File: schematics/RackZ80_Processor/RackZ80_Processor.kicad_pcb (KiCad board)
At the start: 2 copper layers, 160 x 100 mm, 2 parts

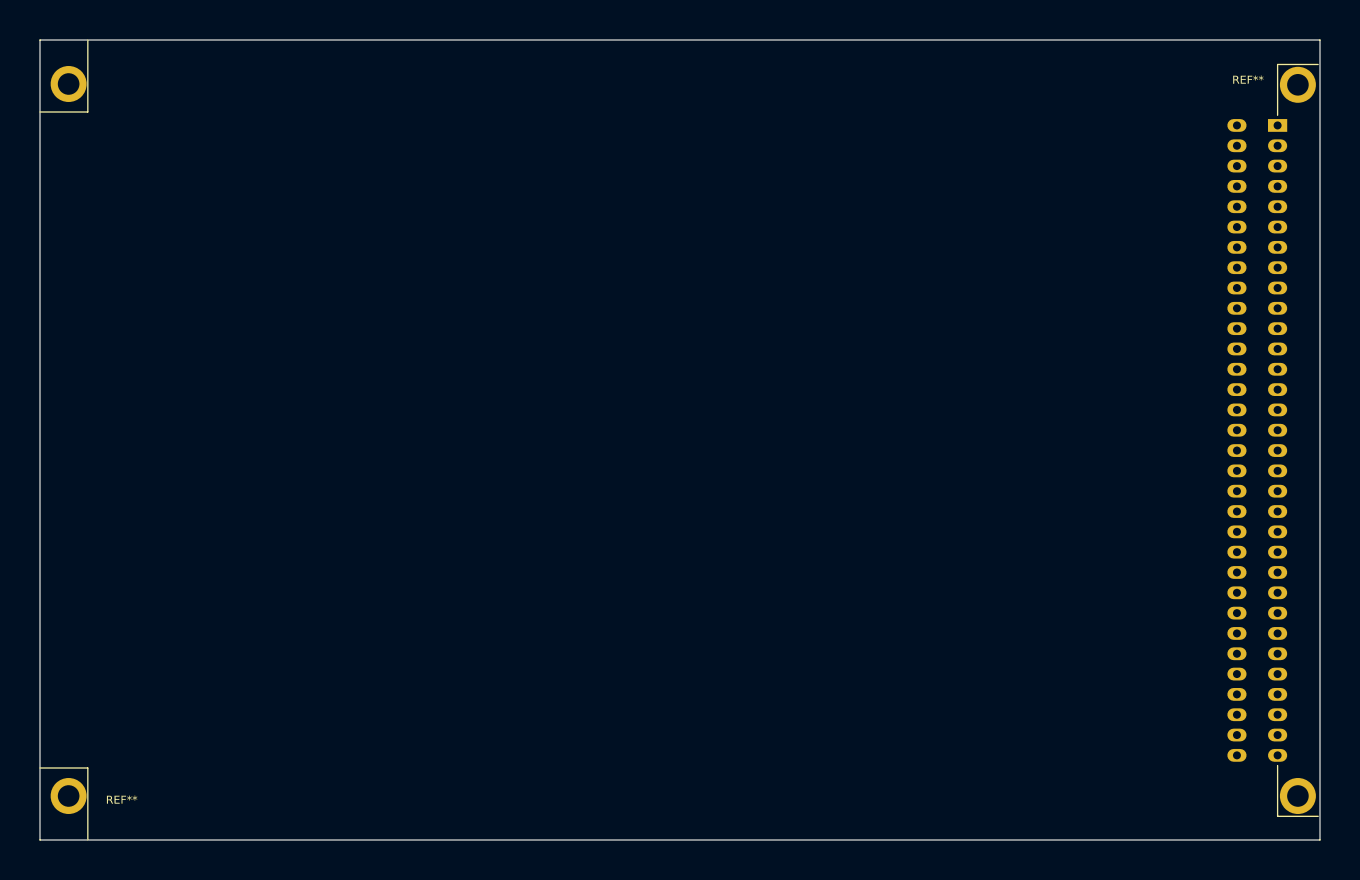
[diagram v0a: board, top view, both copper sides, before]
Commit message: schematics update
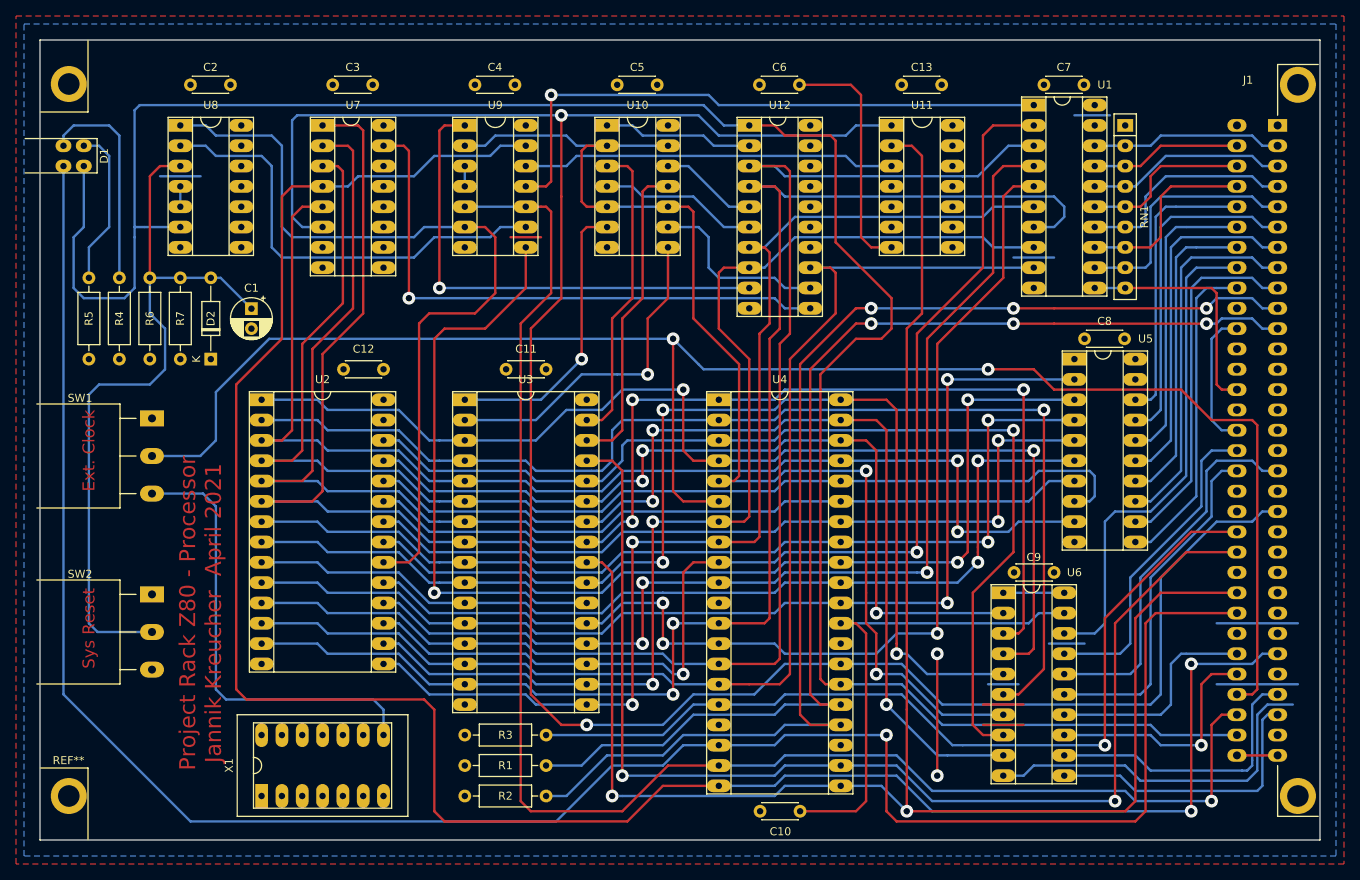
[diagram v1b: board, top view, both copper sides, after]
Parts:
- removed the REF** at (226.8, 138.2)
- added C1: 10uF, Capacitor_THT:CP_Radial_D5.0mm_P2.50mm, F.Cu at (93.2, 71.8)
- added C10: 100nF, Capacitor_THT:C_Disc_D4.3mm_W1.9mm_P5.00mm, F.Cu at (156.8, 134.6)
- added C11: 100nF, Capacitor_THT:C_Disc_D4.3mm_W1.9mm_P5.00mm, F.Cu at (130.1, 79.4)
- added C12: 100nF, Capacitor_THT:C_Disc_D4.3mm_W1.9mm_P5.00mm, F.Cu at (109.7, 79.4)
- added C13: 100nF, Capacitor_THT:C_Disc_D4.3mm_W1.9mm_P5.00mm, F.Cu at (174.5, 43.8)
- added C2: 100nF, Capacitor_THT:C_Disc_D4.3mm_W1.9mm_P5.00mm, F.Cu at (85.6, 43.8)
- added C3: 100nF, Capacitor_THT:C_Disc_D4.3mm_W1.9mm_P5.00mm, F.Cu at (103.4, 43.8)
- added C4: 100nF, Capacitor_THT:C_Disc_D4.3mm_W1.9mm_P5.00mm, F.Cu at (121.2, 43.8)
- added C5: 100nF, Capacitor_THT:C_Disc_D4.3mm_W1.9mm_P5.00mm, F.Cu at (138.9, 43.8)
- added C6: 100nF, Capacitor_THT:C_Disc_D4.3mm_W1.9mm_P5.00mm, F.Cu at (156.7, 43.8)
- added C7: 100nF, Capacitor_THT:C_Disc_D4.3mm_W1.9mm_P5.00mm, F.Cu at (192.3, 43.8)
- added C8: 100nF, Capacitor_THT:C_Disc_D4.3mm_W1.9mm_P5.00mm, F.Cu at (197.4, 75.6)
- added C9: 100nF, Capacitor_THT:C_Disc_D4.3mm_W1.9mm_P5.00mm, F.Cu at (193.6, 104.8)
- added D1: LED, rackz80_footprints:LED_Array_2, F.Cu at (69.7, 51.4)
- added D2: D, Diode_THT:D_DO-35_SOD27_P10.16mm_Horizontal, F.Cu at (88.2, 78.1)
- added J1: ECB_Kontron, rackz80_footprints:Eurocard_DIN41612_C64_Male, F.Cu at (226.8, 138.2)
- added R1: 1k, Resistor_THT:R_Axial_DIN0207_L6.3mm_D2.5mm_P10.16mm_Horizontal, F.Cu at (130.1, 128.9)
- added R2: 1k, Resistor_THT:R_Axial_DIN0207_L6.3mm_D2.5mm_P10.16mm_Horizontal, F.Cu at (130.1, 132.7)
- added R3: 1k, Resistor_THT:R_Axial_DIN0207_L6.3mm_D2.5mm_P10.16mm_Horizontal, F.Cu at (130.1, 125.1)
- added R4: 1k, Resistor_THT:R_Axial_DIN0207_L6.3mm_D2.5mm_P10.16mm_Horizontal, F.Cu at (76.7, 78.1)
- added R5: 1k, Resistor_THT:R_Axial_DIN0207_L6.3mm_D2.5mm_P10.16mm_Horizontal, F.Cu at (72.9, 78.1)
- added R6: 4.7k, Resistor_THT:R_Axial_DIN0207_L6.3mm_D2.5mm_P10.16mm_Horizontal, F.Cu at (80.5, 78.1)
- added R7: 100k, Resistor_THT:R_Axial_DIN0207_L6.3mm_D2.5mm_P10.16mm_Horizontal, F.Cu at (84.3, 67.9)
- added RN1: 1k, Resistor_THT:R_Array_SIP9, F.Cu at (202.4, 48.9)
- added SW1: SW_Clock, rackz80_footprints:SW_MS-500, F.Cu at (80.8, 85.5)
- added SW2: SW_Reset, rackz80_footprints:SW_MS-500, F.Cu at (80.8, 107.5)
- added U1: 74HC245, rackz80_footprints:DIP-20_Socket, F.Cu at (191.0, 46.4)
- added U10: 74LS08, rackz80_footprints:DIP-14_Socket, F.Cu at (137.7, 48.9)
- added U11: 74LS08, rackz80_footprints:DIP-14_Socket, F.Cu at (173.2, 48.9)
- added U12: 74HC273, rackz80_footprints:DIP-20_Socket, F.Cu at (155.5, 48.9)
- added U2: 28C256, rackz80_footprints:DIP-28_Socket_Wide, F.Cu at (94.5, 83.2)
- added U3: 628512, rackz80_footprints:DIP-32_Socket_Wide, F.Cu at (119.9, 83.2)
- added U4: Z80CPU, rackz80_footprints:DIP-40_Socket_Wide, F.Cu at (151.7, 83.2)
- added U5: 74HC245, rackz80_footprints:DIP-20_Socket, F.Cu at (196.1, 78.1)
- added U6: 74HC245, rackz80_footprints:DIP-20_Socket, F.Cu at (187.2, 107.3)
- added U7: 74LS138, rackz80_footprints:DIP-16_Socket, F.Cu at (102.1, 48.9)
- added U8: 74LS14, rackz80_footprints:DIP-14_Socket, F.Cu at (84.3, 48.9)
- added U9: 74LS32, rackz80_footprints:DIP-14_Socket, F.Cu at (119.9, 48.9)
- added X1: 4MHz, rackz80_footprints:DIP-14_Oscillator_Socket, F.Cu at (94.5, 132.7)
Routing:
- net /~M1: track 0.00 -> 285.9 mm, vias 0 -> 2
- net /~RESET: track 0.00 -> 272.8 mm
- net /~IORQ: track 0.00 -> 264.7 mm, vias 0 -> 2
- net /~HALT: track 0.00 -> 258.4 mm, vias 0 -> 1
- net /~RD: track 0.00 -> 250.8 mm, vias 0 -> 2
- net /CLK: track 0.00 -> 215.4 mm, vias 0 -> 2
- net GND: track 0.00 -> 201.3 mm, vias 0 -> 2
- net /~MRQ: track 0.00 -> 192.9 mm, vias 0 -> 1
- net /D2: track 0.00 -> 179.3 mm, vias 0 -> 2
- net /A4: track 0.00 -> 176.6 mm, vias 0 -> 2
- net /D0: track 0.00 -> 172.7 mm
- net /A6: track 0.00 -> 159.9 mm
- net /A5: track 0.00 -> 159.9 mm
- net /D1: track 0.00 -> 153.6 mm
- net /~WAIT: track 0.00 -> 153.6 mm, vias 0 -> 3
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- added copper zone on F.Cu, net +5V
- added copper zone on B.Cu, net GND
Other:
- net class Default: clearance 0.2 -> 0.3175; trace_width 0.25 -> 0.3; via_dia 0.8 -> 1.6; via_drill 0.4 -> 0.8
- rule trace_clearance: 0.2 -> 0.3175
- board text added: "Ext. Clock"
- board text added: "Project Rack Z80 - Processor Jannik Kreucher April 2021"
- board text added: "Sys Reset"

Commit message: migrated kicad 5 to kicad 7
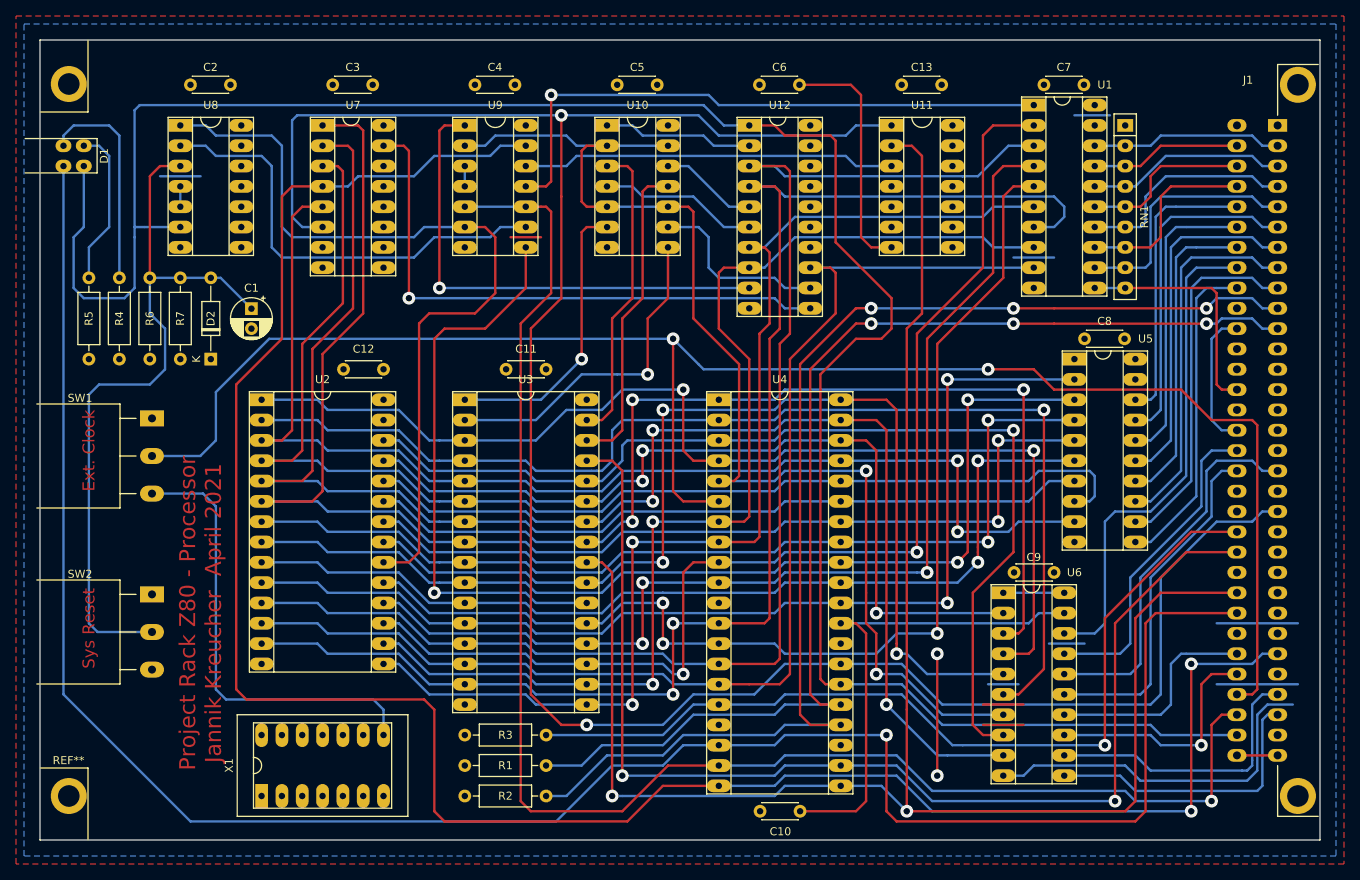
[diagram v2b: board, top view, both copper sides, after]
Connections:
- net /Memory Logic/~RAM_CS renamed /Memory Logic/~{RAM_CS}
- net /Memory Logic/~ROM_CS renamed /Memory Logic/~{ROM_CS}
- net /~BUSRQ renamed /~{BUSRQ}
- net /~BankCS renamed /~{BankCS}
- net /~DIR renamed /~{DIR}
- net /~HALT renamed /~{HALT}
- net /~INT renamed /~{INT}
- net /~IORQ renamed /~{IORQ}
- net /~M1 renamed /~{M1}
- net /~MRQ renamed /~{MRQ}
- net /~RD renamed /~{RD}
- net /~RESET renamed /~{RESET}
- net /~WAIT renamed /~{WAIT}
- net /~WR renamed /~{WR}
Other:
- net class Default removed
